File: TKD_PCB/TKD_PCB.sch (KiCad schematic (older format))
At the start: 49 parts, among them IC1 R5460N233AF-TR-FE, J1 USB2066-05-RBHM-15-STB-00-00-A, J2 Conn_01x06, J3 Conn_02x02_Top_Bottom, J4 Conn_01x07, J5 Conn_01x08, Q1 ZXMN6A09GQTA, Q2 ZXMN6A09GQTA, Q3 S8050, Q4 S8050, SW1 SW_Push, SW2 SW_Push, SW3 SW_SPDT, U1 AMS1117-3.3, U2 FT232RL, U3 LM1085-5.0, U4 ESP32-WROOM-32D, U5 1049

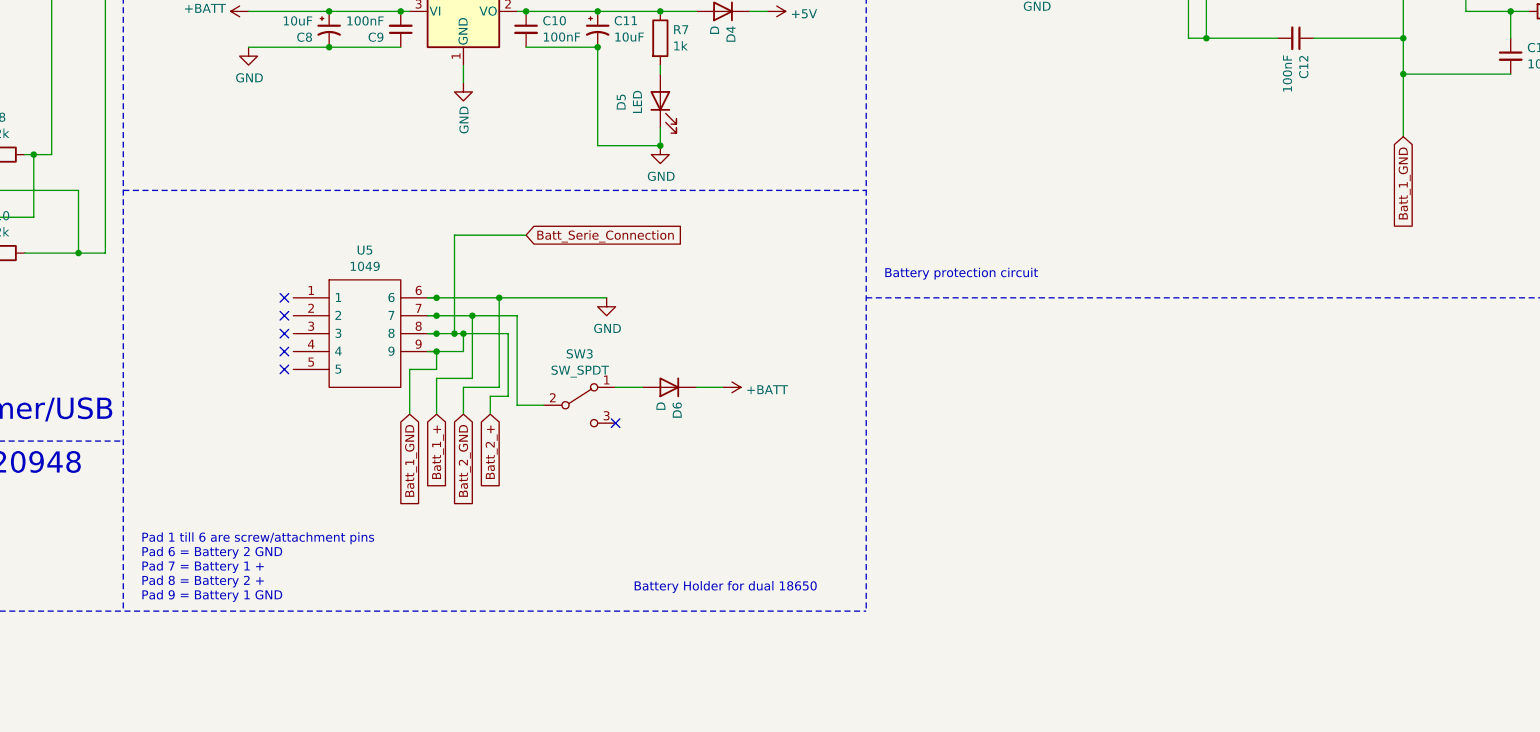
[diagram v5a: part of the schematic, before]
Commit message: made PCB smaller
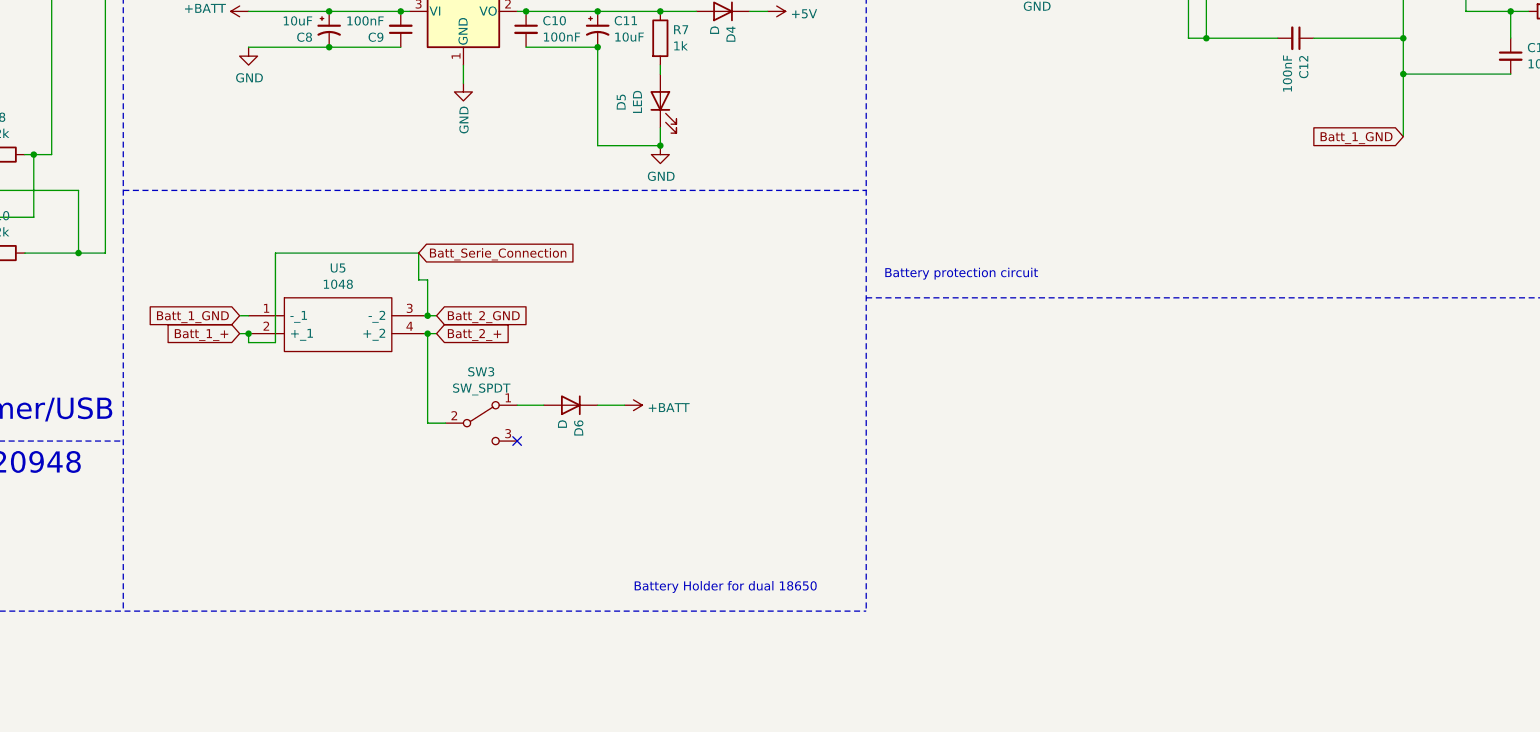
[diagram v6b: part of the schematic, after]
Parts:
- removed U5: 1049, SamacSys_Parts:1049, symbol TKD_PCB-rescue:1049-SamacSys_Parts
- added U5: 1048, 1048, symbol SamacSys_Parts:1048
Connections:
- net Batt_1_+: now also R6.1, U5.2 (+_1), U5.3 (-_2); no longer SW3.2 (B)
- net Batt_1_GND: now also U5.1 (-_1); no longer R6.1
- new net Batt_2_+: SW3.2 (B), U5.4 (+_2)
- no-connect marks 18 -> 13
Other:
- note removed: "Pad 1 till 6 are screw/attachment pins\nPad 6 = Battery 2 GND\nPad 7 = Battery 1 +\nPad 8 = Battery 2 +\nPad 9 = Battery 1 GND"
- moved on the sheet: D6, SW3
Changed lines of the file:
@@
 	4250 5450 4000 5450
-$Comp
-L TKD_PCB-rescue:1049-SamacSys_Parts U?
-U 1 1 5F96C19B
-P 8200 4000
-AR Path="/5F7F5441/5F96C19B" Ref="U?"  Part="1"
-AR Path="/5F96C19B" Ref="U5"  Part="1"
-F 0 "U5" H 8600 4265 50  0000 C CNN
-F 1 "1049" H 8600 4174 50  0000 C CNN
-F 2 "SamacSys_Parts:1049" H 8850 4100 50  0001 L CNN
-F 3 "http://www.keyelco.com/product.cfm/product_id/921" H 8850 4000 50  0001 L CNN
-F 4 "KEYSTONE - 1049 - BATTERY HOLDER, 18650, THROUGH HOLE" H 8850 3900 50  0001 L CNN "Description"
-F 5 "14" H 8850 3800 50  0001 L CNN "Height"
-F 6 "534-1049" H 8850 3700 50  0001 L CNN "Mouser Part Number"
-F 7 "https://www.mouser.co.uk/ProductDetail/Keystone-Electronics/1049?qs=%2F7TOpeL5Mz78b0pqEFIl5w%3D%3D" H 8850 3600 50  0001 L CNN "Mouser Price/Stock"
-F 8 "Keystone Electronics" H 8850 3500 50  0001 L CNN "Manufacturer_Name"
-F 9 "1049" H 8850 3400 50  0001 L CNN "Manufacturer_Part_Number"
-	1    8200 4000
-	1    0    0    -1
-$EndComp
-Wire Wire Line
-	8950 4200 9000 4200
-Wire Wire Line
-	8950 4300 9000 4300
-NoConn ~ 8150 4000
-NoConn ~ 8150 4100
-NoConn ~ 8150 4200
-NoConn ~ 8150 4300
-NoConn ~ 8150 4400
 $Comp
 L power:+BATT #PWR?
 U 1 1 5F96C1A8
-P 10600 4500
+P 10050 4600
 AR Path="/5F7F5441/5F96C1A8" Ref="#PWR?"  Part="1"
 AR Path="/5F96C1A8" Ref="#PWR025"  Part="1"
-F 0 "#PWR025" H 10600 4350 50  0001 C CNN
-F 1 "+BATT" V 10615 4628 50  0000 L CNN
-F 2 "" H 10600 4500 50  0001 C CNN
-F 3 "" H 10600 4500 50  0001 C CNN
-	1    10600 4500
+F 0 "#PWR025" H 10050 4450 50  0001 C CNN
+F 1 "+BATT" V 10065 4728 50  0000 L CNN
+F 2 "" H 10050 4600 50  0001 C CNN
+F 3 "" H 10050 4600 50  0001 C CNN
+	1    10050 4600
 	0    1    1    0
 $EndComp
-$Comp
-L power:GND #PWR?
-U 1 1 5F96C1AE
-P 9950 4000
-AR Path="/5F7F5441/5F96C1AE" Ref="#PWR?"  Part="1"
-AR Path="/5F96C1AE" Ref="#PWR021"  Part="1"
-F 0 "#PWR021" H 9950 3750 50  0001 C CNN
-F 1 "GND" H 9955 3827 50  0000 C CNN
-F 2 "" H 9950 4000 50  0001 C CNN
-F 3 "" H 9950 4000 50  0001 C CNN
-	1    9950 4000
-	1    0    0    -1
-$EndComp
-Wire Wire Line
-	8950 4000 9000 4000
-Wire Wire Line
-	8950 4100 9000 4100
-Wire Wire Line
-	9150 4300 9150 4200
 Wire Notes Line
 	5550 7800 5550 5750
@@
 L Switch:SW_SPDT SW3
 U 1 1 5FA5853B
-P 9800 4600
-F 0 "SW3" H 9800 4885 50  0000 C CNN
-F 1 "SW_SPDT" H 9800 4794 50  0000 C CNN
-F 2 "SamacSys_Parts:AYZ0103AGRLC" H 9800 4600 50  0001 C CNN
-F 3 "~" H 9800 4600 50  0001 C CNN
-F 4 " 611-AYZ0103AGRLC " H 9800 4600 50  0001 C CNN "Mouser Part Number"
-	1    9800 4600
-	1    0    0    -1
-$EndComp
-Wire Wire Line
-	10000 4500 10150 4500
-Wire Wire Line
-	9450 4100 9450 4600
+P 9250 4700
+F 0 "SW3" H 9250 4985 50  0000 C CNN
+F 1 "SW_SPDT" H 9250 4894 50  0000 C CNN
+F 2 "SamacSys_Parts:AYZ0103AGRLC" H 9250 4700 50  0001 C CNN
+F 3 "~" H 9250 4700 50  0001 C CNN
+F 4 " 611-AYZ0103AGRLC " H 9250 4700 50  0001 C CNN "Mouser Part Number"
+	1    9250 4700
+	1    0    0    -1
+$EndComp
 Wire Wire Line
 	9450 4600 9600 4600
-NoConn ~ 10000 4700
-Connection ~ 9000 4000
-Wire Wire Line
-	9000 4000 9350 4000
-Connection ~ 9000 4100
-Wire Wire Line
-	9000 4100 9200 4100
-Connection ~ 9000 4200
-Wire Wire Line
-	9000 4200 9100 4200
-Connection ~ 9000 4300
-Wire Wire Line
-	9000 4300 9150 4300
-Text GLabel 8850 4650 3    50   Input ~ 0
+NoConn ~ 9450 4800
+Text GLabel 7900 4100 0    50   Input ~ 0
 Batt_1_GND
-Text GLabel 9000 4650 3    50   Input ~ 0
+Text GLabel 7900 4200 0    50   Input ~ 0
 Batt_1_+
-Text GLabel 9150 4650 3    50   Input ~ 0
+Text GLabel 9000 4100 2    50   Input ~ 0
 Batt_2_GND
-Text GLabel 9300 4650 3    50   Input ~ 0
+Text GLabel 9000 4200 2    50   Input ~ 0
 Batt_2_+
-Wire Wire Line
-	9000 4300 9000 4400
-Wire Wire Line
-	9000 4400 8850 4400
-Wire Wire Line
-	8850 4400 8850 4650
-Wire Wire Line
-	9200 4100 9200 4450
-Wire Wire Line
-	9200 4450 9000 4450
-Wire Wire Line
-	9000 4450 9000 4650
-Connection ~ 9200 4100
-Wire Wire Line
-	9200 4100 9450 4100
-Connection ~ 9350 4000
-Wire Wire Line
-	9350 4000 9950 4000
-Wire Wire Line
-	9350 4000 9350 4500
-Wire Wire Line
-	9350 4500 9150 4500
-Wire Wire Line
-	9150 4500 9150 4650
-Wire Wire Line
-	9400 4200 9400 4550
-Wire Wire Line
-	9400 4550 9300 4550
-Wire Wire Line
-	9300 4550 9300 4650
-Connection ~ 9150 4200
-Wire Wire Line
-	9150 4200 9400 4200
 Connection ~ 9900 2600
 Connection ~ 10250 3150
@@
 L Device:D D6
 U 1 1 6028C3AD
-P 10300 4500
-F 0 "D6" V 10254 4580 50  0000 L CNN
-F 1 "D" V 10345 4580 50  0000 L CNN
-F 2 "Diode_SMD:D_0805_2012Metric_Pad1.15x1.40mm_HandSolder" H 10300 4500 50  0001 C CNN
-F 3 "~" H 10300 4500 50  0001 C CNN
-F 4 "C72036" H 10300 4500 50  0001 C CNN "LCSC"
-	1    10300 4500
+P 9750 4600
+F 0 "D6" V 9704 4680 50  0000 L CNN
+F 1 "D" V 9795 4680 50  0000 L CNN
+F 2 "Diode_SMD:D_0805_2012Metric_Pad1.15x1.40mm_HandSolder" H 9750 4600 50  0001 C CNN
+F 3 "~" H 9750 4600 50  0001 C CNN
+F 4 "C72036" H 9750 4600 50  0001 C CNN "LCSC"
+	1    9750 4600
 	-1   0    0    1
 $EndComp
 Wire Wire Line
-	10450 4500 10600 4500
+	9900 4600 10050 4600
 $Comp
 L Device:D D4
@@
 Wire Wire Line
 	14750 2400 15000 2400
-Wire Wire Line
-	9100 4200 9100 3650
-Connection ~ 9100 4200
-Wire Wire Line
-	9100 4200 9150 4200
-Text GLabel 9500 3650 2    50   Input ~ 0
+Text GLabel 8900 3750 2    50   Input ~ 0
 Batt_Serie_Connection
-Wire Wire Line
-	9100 3650 9500 3650
 Text GLabel 15850 2400 3    50   Input ~ 0
 Batt_Serie_Connection
@@
 Wire Wire Line
 	13100 2000 13250 2000
-Text GLabel 14400 3100 3    50   Input ~ 0
-Batt_1_GND
 Wire Wire Line
 	14400 2750 14400 3100
@@
 Text Notes 10100 5650 0    50   ~ 0
 Battery Holder for dual 18650
-Text Notes 7350 5700 0    50   ~ 0
-Pad 1 till 6 are screw/attachment pins\nPad 6 = Battery 2 GND\nPad 7 = Battery 1 +\nPad 8 = Battery 2 +\nPad 9 = Battery 1 GND
 Wire Notes Line
 	11400 4000 16100 4000
@@
 	3000 1450 3000 1550
 Connection ~ 3000 1450
+$Comp
+L SamacSys_Parts:1048 U5
+U 1 1 60E08EC3
+P 7950 4100
+F 0 "U5" H 8450 4365 50  0000 C CNN
+F 1 "1048" H 8450 4274 50  0000 C CNN
+F 2 "1048" H 8800 4200 50  0001 L CNN
+F 3 "http://www.keyelco.com/product-pdf.cfm?p=920" H 8800 4100 50  0001 L CNN
+F 4 "KEYSTONE - 1048 - BATTERY HOLDER, 18650 LI-ION, 2CELL, SMD" H 8800 4000 50  0001 L CNN "Description"
+F 5 "" H 8800 3900 50  0001 L CNN "Height"
+F 6 "534-1048" H 8800 3800 50  0001 L CNN "Mouser Part Number"
+F 7 "https://www.mouser.co.uk/ProductDetail/Keystone-Electronics/1048?qs=%2F7TOpeL5Mz5jXkg8vI8Dyw%3D%3D" H 8800 3700 50  0001 L CNN "Mouser Price/Stock"
+F 8 "Keystone Electronics" H 8800 3600 50  0001 L CNN "Manufacturer_Name"
+F 9 "1048" H 8800 3500 50  0001 L CNN "Manufacturer_Part_Number"
+	1    7950 4100
+	1    0    0    -1
+$EndComp
+Wire Wire Line
+	8100 3750 8900 3750
+Wire Wire Line
+	7900 4100 7950 4100
+Wire Wire Line
+	7950 4200 7900 4200
+Wire Wire Line
+	7950 4200 7950 4250
+Wire Wire Line
+	7950 4250 8100 4250
+Wire Wire Line
+	8100 4250 8100 3750
+Connection ~ 7950 4200
+Wire Wire Line
+	8950 4100 9000 4100
+Wire Wire Line
+	8950 4200 9000 4200
+Wire Wire Line
+	8950 4200 8950 4700
+Wire Wire Line
+	8950 4700 9050 4700
+Connection ~ 8950 4200
+Wire Wire Line
+	8950 4100 8950 3900
+Wire Wire Line
+	8950 3900 8900 3900
+Connection ~ 8950 4100
+Wire Wire Line
+	8900 3750 8900 3900
+Text GLabel 14400 3100 0    50   Input ~ 0
+Batt_1_GND
 $EndSCHEMATC

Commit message: Gyro PCB created and finished ready to order
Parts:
- J1: symbol SamacSys_Parts:USB2066-05-RBHM-15-STB-00-00-A -> TKD_PCB-rescue:USB2066-05-RBHM-15-STB-00-00-A-SamacSys_Parts
- U5: symbol SamacSys_Parts:1048 -> TKD_PCB-rescue:1048-SamacSys_Parts
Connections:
- net VSPIMISO: no longer J2.4 (Pin_4)
- net VSPIMOSI: no longer J2.3 (Pin_3)
- new net VSPI_SDI: J2.4 (Pin_4)
- new net VSPI_SDO: J2.3 (Pin_3)
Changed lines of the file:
@@
 	4000 5250 4250 5250
 Text Label 4000 5250 2    50   ~ 0
-VSPIMOSI
+VSPI_SDO
 Text Label 2650 2850 0    50   ~ 0
 VSPIMISO
@@
 	2500 2850 2650 2850
 Text Label 4000 5350 2    50   ~ 0
-VSPIMISO
+VSPI_SDI
 Wire Wire Line
 	4250 5350 4000 5350
@@
 	7250 3400 11400 3400
 $Comp
-L SamacSys_Parts:USB2066-05-RBHM-15-STB-00-00-A J1
+L TKD_PCB-rescue:USB2066-05-RBHM-15-STB-00-00-A-SamacSys_Parts J1
 U 1 1 60DB3BDD
 P 3900 1550
@@
 Connection ~ 3000 1450
 $Comp
-L SamacSys_Parts:1048 U5
+L TKD_PCB-rescue:1048-SamacSys_Parts U5
 U 1 1 60E08EC3
 P 7950 4100

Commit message: Final check before ordering
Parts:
- removed J3: Conn_02x02_Top_Bottom, Connector_PinHeader_2.54mm:PinHeader_2x02_P2.54mm_Vertical, symbol Connector_Generic:Conn_02x02_Top_Bottom
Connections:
- net VSPIMISO is gone; now on net VSPI_SDI: U4.31 (IO19)
- net VSPIMOSI is gone; now on net VSPI_SDO: U4.37 (IO23)
- net +5V: no longer C1.1, C2.1, U2.20 (VCC)
- net USB_5V: now reaches D2.2 (A), J1.1
- net USB_5V: now also C1.1, C2.1, U2.20 (VCC)
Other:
- moved on the sheet: D2
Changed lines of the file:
@@
 Wire Wire Line
 	3900 1150 4050 1150
-Text Label 4000 2000 2    50   ~ 0
+Text Label 3900 1850 2    50   ~ 0
 USB_5V
 Wire Wire Line
@@
 Wire Wire Line
 	6700 1250 6800 1250
-Text Label 7850 950  2    50   ~ 0
-USB_5V
 $Comp
 L power:GND #PWR06
@@
 L Device:D D2
 U 1 1 5F4EC909
-P 4050 1850
-F 0 "D2" V 4004 1930 50  0000 L CNN
-F 1 "D" V 4095 1930 50  0000 L CNN
-F 2 "Diode_SMD:D_SOD-123" H 4050 1850 50  0001 C CNN
-F 3 "~" H 4050 1850 50  0001 C CNN
-F 4 "C151892" V 4050 1850 50  0001 C CNN "LCSC"
-	1    4050 1850
+P 4050 2000
+F 0 "D2" V 4004 2080 50  0000 L CNN
+F 1 "D" V 4095 2080 50  0000 L CNN
+F 2 "Diode_SMD:D_SOD-123" H 4050 2000 50  0001 C CNN
+F 3 "~" H 4050 2000 50  0001 C CNN
+F 4 "C151892" V 4050 2000 50  0001 C CNN "LCSC"
+	1    4050 2000
 	0    -1   -1   0
 $EndComp
-Wire Wire Line
-	4050 2000 4000 2000
 Wire Wire Line
 	9200 1300 9200 1400
@@
 L power:+5V #PWR03
 U 1 1 5F47548A
-P 7850 1050
-F 0 "#PWR03" H 7850 900 50  0001 C CNN
-F 1 "+5V" V 7865 1178 50  0000 L CNN
-F 2 "" H 7850 1050 50  0001 C CNN
-F 3 "" H 7850 1050 50  0001 C CNN
-	1    7850 1050
+P 7850 1000
+F 0 "#PWR03" H 7850 850 50  0001 C CNN
+F 1 "+5V" V 7865 1128 50  0000 L CNN
+F 2 "" H 7850 1000 50  0001 C CNN
+F 3 "" H 7850 1000 50  0001 C CNN
+	1    7850 1000
 	0    -1   -1   0
 $EndComp
@@
 Wire Wire Line
 	8800 1000 8400 1000
-Wire Wire Line
-	8000 1000 8000 1050
-Wire Wire Line
-	8000 1050 7850 1050
-Wire Wire Line
-	8000 1000 8400 1000
-Wire Wire Line
-	8000 1000 8000 950
-Wire Wire Line
-	8000 950  7850 950
-Connection ~ 8000 1000
 $Comp
 L Device:C_Small C5
@@
 	4250 5150 4000 5150
 Text Label 2650 3150 0    50   ~ 0
-VSPIMOSI
+VSPI_SDO
 Wire Wire Line
 	2500 3150 2650 3150
 Wire Wire Line
 	4000 5250 4250 5250
-Text Label 4000 5250 2    50   ~ 0
-VSPI_SDO
 Text Label 2650 2850 0    50   ~ 0
-VSPIMISO
+VSPI_SDI
 Wire Wire Line
 	2500 2850 2650 2850
-Text Label 4000 5350 2    50   ~ 0
-VSPI_SDI
 Wire Wire Line
 	4250 5350 4000 5350
@@
 	1150 7100 1000 7100
 $Comp
-L Connector_Generic:Conn_02x02_Top_Bottom J3
-U 1 1 5FA381F6
-P 3950 6450
-F 0 "J3" H 4000 6667 50  0000 C CNN
-F 1 "Conn_02x02_Top_Bottom" H 4000 6576 50  0000 C CNN
-F 2 "Connector_PinHeader_2.54mm:PinHeader_2x02_P2.54mm_Vertical" H 3950 6450 50  0001 C CNN
-F 3 "~" H 3950 6450 50  0001 C CNN
-	1    3950 6450
-	1    0    0    -1
-$EndComp
-$Comp
-L power:+3.3V #PWR028
-U 1 1 5FA38FF5
-P 3400 6450
-F 0 "#PWR028" H 3400 6300 50  0001 C CNN
-F 1 "+3.3V" H 3415 6623 50  0000 C CNN
-F 2 "" H 3400 6450 50  0001 C CNN
-F 3 "" H 3400 6450 50  0001 C CNN
-	1    3400 6450
-	1    0    0    -1
-$EndComp
-$Comp
-L power:+5V #PWR030
-U 1 1 5FA39FDE
-P 3250 6550
-F 0 "#PWR030" H 3250 6400 50  0001 C CNN
-F 1 "+5V" H 3265 6723 50  0000 C CNN
-F 2 "" H 3250 6550 50  0001 C CNN
-F 3 "" H 3250 6550 50  0001 C CNN
-	1    3250 6550
-	1    0    0    -1
-$EndComp
-Wire Wire Line
-	3750 6450 3400 6450
-Wire Wire Line
-	3750 6550 3250 6550
-$Comp
-L power:GND #PWR029
-U 1 1 5FA48CD0
-P 4500 6500
-F 0 "#PWR029" H 4500 6250 50  0001 C CNN
-F 1 "GND" H 4505 6327 50  0000 C CNN
-F 2 "" H 4500 6500 50  0001 C CNN
-F 3 "" H 4500 6500 50  0001 C CNN
-	1    4500 6500
-	1    0    0    -1
-$EndComp
-Wire Wire Line
-	4250 6450 4350 6450
-Wire Wire Line
-	4350 6450 4350 6500
-Wire Wire Line
-	4350 6500 4500 6500
-Wire Wire Line
-	4250 6550 4350 6550
-Wire Wire Line
-	4350 6550 4350 6500
-Connection ~ 4350 6500
-$Comp
 L Switch:SW_SPDT SW3
 U 1 1 5FA5853B
@@
 $EndComp
 Wire Wire Line
-	4050 1700 4050 1550
-Wire Wire Line
 	4050 1550 3900 1550
 Wire Wire Line
@@
 Text GLabel 14400 3100 0    50   Input ~ 0
 Batt_1_GND
+Wire Wire Line
+	4050 1550 4050 1850
+Wire Wire Line
+	3900 1850 4050 1850
+Connection ~ 4050 1850
+Wire Wire Line
+	7850 1000 8400 1000
+$Comp
+L power:+5V #PWR?
+U 1 1 6113B4F2
+P 3900 2250
+F 0 "#PWR?" H 3900 2100 50  0001 C CNN
+F 1 "+5V" V 3915 2378 50  0000 L CNN
+F 2 "" H 3900 2250 50  0001 C CNN
+F 3 "" H 3900 2250 50  0001 C CNN
+	1    3900 2250
+	0    -1   -1   0
+$EndComp
+Wire Wire Line
+	4050 2150 4050 2250
+Wire Wire Line
+	4050 2250 3900 2250
+Text Label 4000 5350 2    50   ~ 0
+VSPI_SDI
+Text Label 4000 5250 2    50   ~ 0
+VSPI_SDO
 $EndSCHEMATC
